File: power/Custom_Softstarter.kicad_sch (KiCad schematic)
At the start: 7 parts, among them K1 Relay, Q2 IRFZ44N

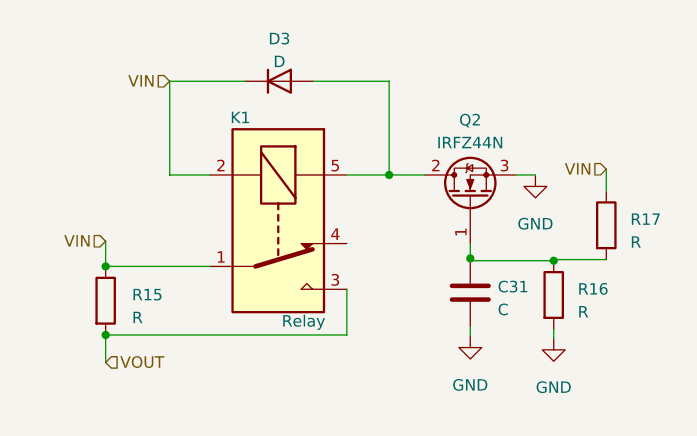
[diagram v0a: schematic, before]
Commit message: Feat: Added draft resistance and capacitance to softstarter
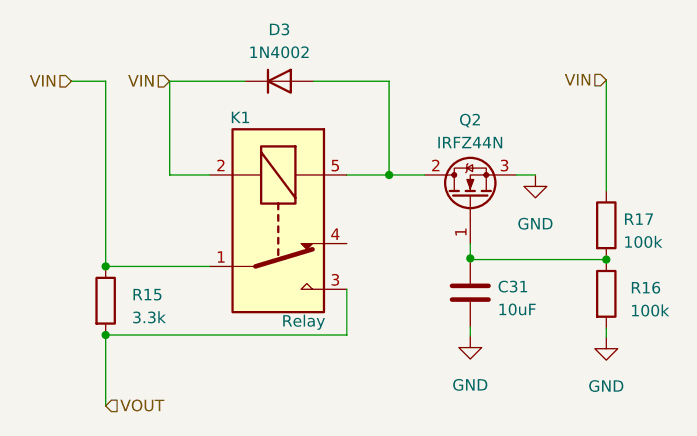
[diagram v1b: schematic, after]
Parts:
- C31: value C -> 10uF
- D3: value D -> 1N4002
- R15: value R -> 3.3k
- R16, R17: value R -> 100k
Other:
- moved on the sheet: R16
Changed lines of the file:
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@@
   (junction (at 118.999 111.379) (diameter 0) (color 0 0 0 0)
   )
-  (junction (at 168.783 103.124) (diameter 0) (color 0 0 0 0)
+  (junction (at 174.625 102.997) (diameter 0) (color 0 0 0 0)
   )
   (junction (at 118.999 103.759) (diameter 0) (color 0 0 0 0)
@@
   (junction (at 150.495 93.599) (diameter 0) (color 0 0 0 0)
   )
+  (wire (pts (xy 164.592 93.599) (xy 166.751 93.599))
+    (stroke (width 0) (type default))
+  )
+  (wire (pts (xy 150.495 93.599) (xy 154.432 93.599))
+    (stroke (width 0) (type default))
+  )
+  (wire (pts (xy 159.512 102.87) (xy 159.512 102.997))
+    (stroke (width 0) (type default))
+  )
+  (wire (pts (xy 118.999 103.759) (xy 130.556 103.759))
+    (stroke (width 0) (type default))
+  )
+  (wire (pts (xy 118.999 111.379) (xy 118.999 119.253))
+    (stroke (width 0) (type default))
+  )
+  (wire (pts (xy 118.999 83.185) (xy 118.999 103.759))
+    (stroke (width 0) (type default))
+  )
+  (wire (pts (xy 150.495 83.185) (xy 142.113 83.185))
+    (stroke (width 0) (type default))
+  )
+  (wire (pts (xy 115.189 83.185) (xy 118.999 83.185))
+    (stroke (width 0) (type default))
+  )
+  (wire (pts (xy 174.625 83.058) (xy 174.625 95.377))
+    (stroke (width 0) (type default))
+  )
+  (wire (pts (xy 126.111 93.599) (xy 130.556 93.599))
+    (stroke (width 0) (type default))
+  )
+  (wire (pts (xy 174.625 110.617) (xy 174.625 111.633))
+    (stroke (width 0) (type default))
+  )
+  (wire (pts (xy 150.495 93.599) (xy 150.495 83.185))
+    (stroke (width 0) (type default))
+  )
+  (wire (pts (xy 118.999 111.379) (xy 145.796 111.379))
+    (stroke (width 0) (type default))
+  )
+  (wire (pts (xy 145.796 93.599) (xy 150.495 93.599))
+    (stroke (width 0) (type default))
+  )
+  (wire (pts (xy 126.111 83.185) (xy 126.111 93.599))
+    (stroke (width 0) (type default))
+  )
+  (wire (pts (xy 174.625 102.997) (xy 159.512 102.997))
+    (stroke (width 0) (type default))
+  )
+  (wire (pts (xy 134.493 83.185) (xy 126.111 83.185))
+    (stroke (width 0) (type default))
+  )
+  (wire (pts (xy 159.512 110.49) (xy 159.512 111.506))
+    (stroke (width 0) (type default))
+  )
+  (wire (pts (xy 145.796 111.379) (xy 145.796 106.299))
+    (stroke (width 0) (type default))
+  )
   (wire (pts (xy 159.512 101.219) (xy 159.512 102.87))
     (stroke (width 0) (type default))
   )
-  (wire (pts (xy 164.592 93.599) (xy 166.751 93.599))
-    (stroke (width 0) (type default))
-  )
-  (wire (pts (xy 150.495 93.599) (xy 154.432 93.599))
-    (stroke (width 0) (type default))
-  )
-  (wire (pts (xy 118.999 103.759) (xy 130.556 103.759))
-    (stroke (width 0) (type default))
-  )
-  (wire (pts (xy 168.783 102.997) (xy 168.783 103.124))
-    (stroke (width 0) (type default))
-  )
-  (wire (pts (xy 118.999 111.379) (xy 118.999 114.427))
-    (stroke (width 0) (type default))
-  )
-  (wire (pts (xy 118.999 100.965) (xy 118.999 103.759))
-    (stroke (width 0) (type default))
-  )
-  (wire (pts (xy 150.495 83.185) (xy 142.113 83.185))
-    (stroke (width 0) (type default))
-  )
-  (wire (pts (xy 174.625 92.964) (xy 174.625 95.377))
-    (stroke (width 0) (type default))
-  )
-  (wire (pts (xy 126.111 93.599) (xy 130.556 93.599))
-    (stroke (width 0) (type default))
-  )
-  (wire (pts (xy 168.783 110.744) (xy 168.783 111.76))
-    (stroke (width 0) (type default))
-  )
-  (wire (pts (xy 150.495 93.599) (xy 150.495 83.185))
-    (stroke (width 0) (type default))
-  )
-  (wire (pts (xy 174.625 102.997) (xy 168.783 102.997))
-    (stroke (width 0) (type default))
-  )
-  (wire (pts (xy 168.783 103.124) (xy 159.512 103.124))
-    (stroke (width 0) (type default))
-  )
-  (wire (pts (xy 118.999 111.379) (xy 145.796 111.379))
-    (stroke (width 0) (type default))
-  )
-  (wire (pts (xy 145.796 93.599) (xy 150.495 93.599))
-    (stroke (width 0) (type default))
-  )
-  (wire (pts (xy 126.111 83.185) (xy 126.111 93.599))
-    (stroke (width 0) (type default))
-  )
-  (wire (pts (xy 134.493 83.185) (xy 126.111 83.185))
-    (stroke (width 0) (type default))
-  )
-  (wire (pts (xy 159.512 110.49) (xy 159.512 111.506))
-    (stroke (width 0) (type default))
-  )
-  (wire (pts (xy 159.512 103.124) (xy 159.512 102.87))
-    (stroke (width 0) (type default))
-  )
-  (wire (pts (xy 145.796 111.379) (xy 145.796 106.299))
-    (stroke (width 0) (type default))
-  )
-  (hierarchical_label "VIN" (shape input) (at 174.625 92.964 180) (fields_autoplaced)
+  (hierarchical_label "VIN" (shape input) (at 174.625 83.058 180) (fields_autoplaced)
     (effects (font (size 1.27 1.27)) (justify right))
   )
@@
     (effects (font (size 1.27 1.27)) (justify right))
   )
-  (hierarchical_label "VOUT" (shape input) (at 118.999 114.427 0) (fields_autoplaced)
+  (hierarchical_label "VOUT" (shape input) (at 118.999 119.253 0) (fields_autoplaced)
     (effects (font (size 1.27 1.27)) (justify left))
   )
-  (hierarchical_label "VIN" (shape input) (at 118.999 100.965 180) (fields_autoplaced)
+  (hierarchical_label "VIN" (shape input) (at 115.189 83.185 180) (fields_autoplaced)
     (effects (font (size 1.27 1.27)) (justify right))
   )
-  (symbol (lib_id "Device:R") (at 168.783 106.934 0) (unit 1)
-    (in_bom yes) (on_board yes) (dnp no) (fields_autoplaced)
-    (property "Reference" "R16" (at 171.45 106.299 0)
-      (effects (font (size 1.27 1.27)) (justify left))
-    )
-    (property "Value" "R" (at 171.45 108.839 0)
-      (effects (font (size 1.27 1.27)) (justify left))
-    )
-    (property "Footprint" "" (at 167.005 106.934 90)
-      (effects (font (size 1.27 1.27)) hide)
-    )
-    (property "Datasheet" "~" (at 168.783 106.934 0)
+  (symbol (lib_id "Device:R") (at 174.625 106.807 0) (unit 1)
+    (in_bom yes) (on_board yes) (dnp no) (fields_autoplaced)
+    (property "Reference" "R16" (at 177.292 106.172 0)
+      (effects (font (size 1.27 1.27)) (justify left))
+    )
+    (property "Value" "100k" (at 177.292 108.712 0)
+      (effects (font (size 1.27 1.27)) (justify left))
+    )
+    (property "Footprint" "" (at 172.847 106.807 90)
+      (effects (font (size 1.27 1.27)) hide)
+    )
+    (property "Datasheet" "~" (at 174.625 106.807 0)
       (effects (font (size 1.27 1.27)) hide)
     )
@@
       (effects (font (size 1.27 1.27)) (justify left))
     )
-    (property "Value" "C" (at 162.56 108.585 0)
+    (property "Value" "10uF" (at 162.56 108.585 0)
       (effects (font (size 1.27 1.27)) (justify left))
     )
@@
   (symbol (lib_id "Device:D") (at 138.303 83.185 0) (unit 1)
     (in_bom yes) (on_board yes) (dnp no) (fields_autoplaced)
-    (property "Reference" "D3" (at 138.303 78.486 0)
-      (effects (font (size 1.27 1.27)))
-    )
-    (property "Value" "D" (at 138.303 81.026 0)
+    (property "Reference" "D3" (at 138.303 77.47 0)
+      (effects (font (size 1.27 1.27)))
+    )
+    (property "Value" "1N4002" (at 138.303 80.01 0)
       (effects (font (size 1.27 1.27)))
     )
@@
   (symbol (lib_id "Device:R") (at 174.625 99.187 0) (unit 1)
     (in_bom yes) (on_board yes) (dnp no) (fields_autoplaced)
-    (property "Reference" "R17" (at 177.292 98.552 0)
-      (effects (font (size 1.27 1.27)) (justify left))
-    )
-    (property "Value" "R" (at 177.292 101.092 0)
+    (property "Reference" "R17" (at 176.53 98.552 0)
+      (effects (font (size 1.27 1.27)) (justify left))
+    )
+    (property "Value" "100k" (at 176.53 101.092 0)
       (effects (font (size 1.27 1.27)) (justify left))
     )
@@
       (effects (font (size 1.27 1.27)) (justify left))
     )
-    (property "Value" "R" (at 121.92 109.474 0)
+    (property "Value" "3.3k" (at 121.92 109.474 0)
       (effects (font (size 1.27 1.27)) (justify left))
     )
@@
     )
   )
-  (symbol (lib_id "power:GND") (at 168.783 111.76 0) (unit 1)
-    (in_bom yes) (on_board yes) (dnp no) (fields_autoplaced)
-    (property "Reference" "#PWR024" (at 168.783 118.11 0)
-      (effects (font (size 1.27 1.27)) hide)
-    )
-    (property "Value" "GND" (at 168.783 117.221 0)
-      (effects (font (size 1.27 1.27)))
-    )
-    (property "Footprint" "" (at 168.783 111.76 0)
-      (effects (font (size 1.27 1.27)) hide)
-    )
-    (property "Datasheet" "" (at 168.783 111.76 0)
-      (effects (font (size 1.27 1.27)) hide)
-    )
+  (symbol (lib_id "power:GND") (at 174.625 111.633 0) (unit 1)
+    (in_bom yes) (on_board yes) (dnp no) (fields_autoplaced)
+    (property "Reference" "#PWR024" (at 174.625 117.983 0)
+      (effects (font (size 1.27 1.27)) hide)
+    )
+    (property "Value" "GND" (at 174.625 117.094 0)
+      (effects (font (size 1.27 1.27)))
+    )
+    (property "Footprint" "" (at 174.625 111.633 0)
+      (effects (font (size 1.27 1.27)) hide)
+    )
+    (property "Datasheet" "" (at 174.625 111.633 0)
+      (effects (font (size 1.27 1.27)) hide)
+    )

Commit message: Feat: assigned IC footprints, removed softstarter
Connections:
- no-connect marks 0 -> 1
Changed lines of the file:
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@@
   (junction (at 150.495 93.599) (diameter 0) (color 0 0 0 0)
   )
+  (no_connect (at 145.796 101.219))
   (wire (pts (xy 164.592 93.599) (xy 166.751 93.599))
     (stroke (width 0) (type default))
